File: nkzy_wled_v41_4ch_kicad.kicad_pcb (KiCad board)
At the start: 2 copper layers, 61 x 39 mm, 68 parts, among them CN1 1x3P_3.96mm_RA_Conn, CN2 1x3P_3.96mm_RA_Conn, CN3 1x3P_3.96mm_RA_Conn, CN4 1x3P_3.96mm_RA_Conn, CN5 1x2P_3.96mm_RA_Conn, J1 1x2P_2.54mm_RA_Conn, J2 HC-2510-3AW, K1 12VDC_SPDT, Q1 AO3401, U1 ESP32-WROOM-32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

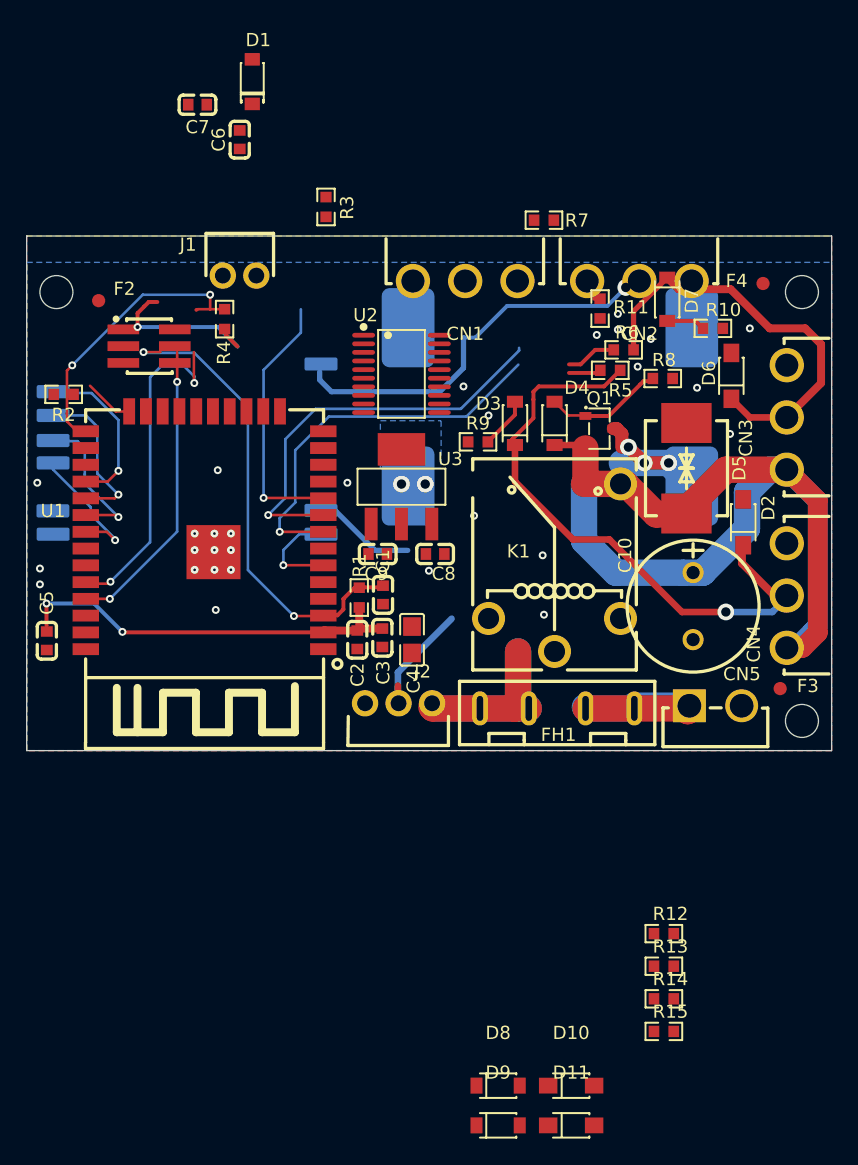
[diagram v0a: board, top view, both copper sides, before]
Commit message: Routed 4 ch pcb and resolved all DRC
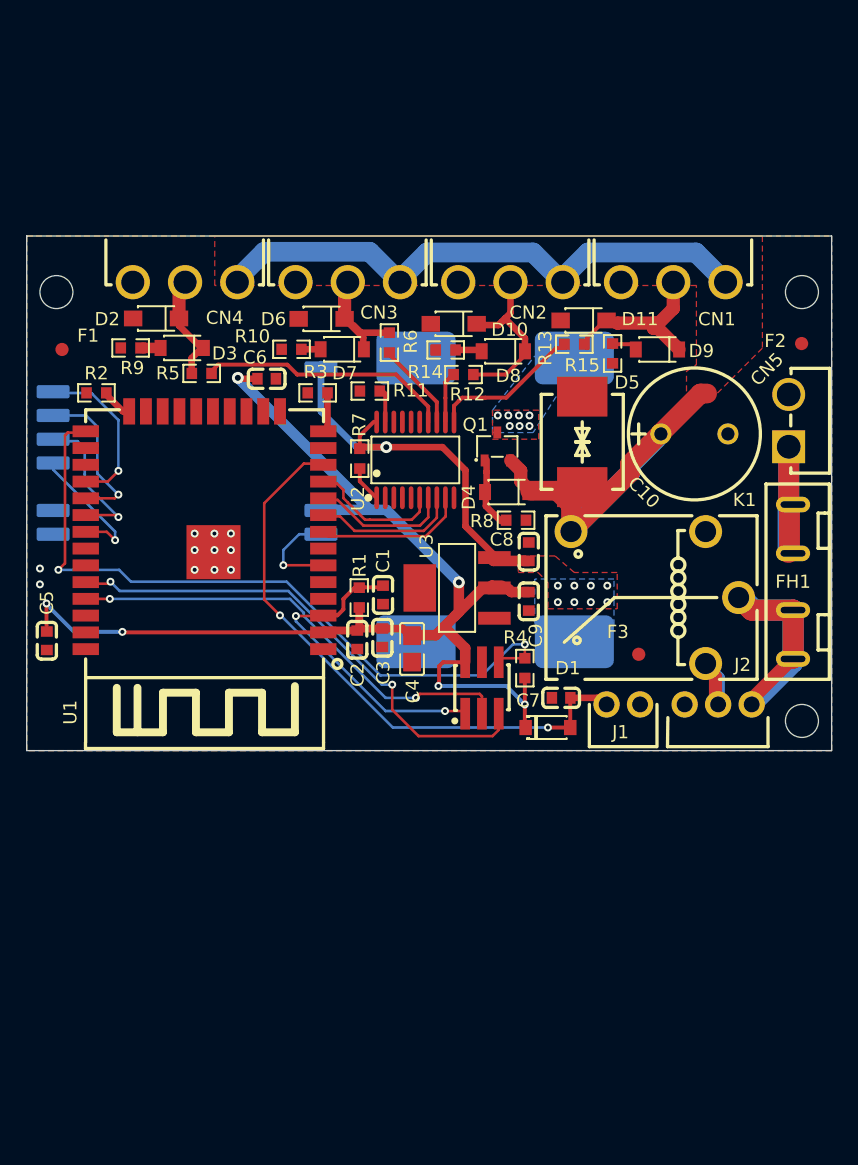
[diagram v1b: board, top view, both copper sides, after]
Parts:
- removed the F2 at (5.45, 2.90)
- removed P1, P2, P3, P4, P5, P6, P7, P8, P9: ~, nkzy_wled_lib:Pad_2.5x1mm
- added F1: Fiducial_1mm_Mask2mm, Fiducial:Fiducial_1mm_Mask2mm, F.Cu at (2.67, 6.60)
- added J3: ~, nkzy_wled_lib:nkzy_addon_footprint, B.Cu at (12.2, 14.3)
- moved D11 61.0 mm to (42.2, 4.40), turned to 180 degrees
- moved D9 60.0 mm to (47.8, 6.60), turned to 180 degrees
- moved D10 58.4 mm to (32.4, 4.65), turned to 180 degrees
- moved D8 55.7 mm to (36.1, 6.74), turned to 180 degrees
- moved D1 53.8 mm to (39.5, 35.2), turned to 0 degrees
- moved C7 52.7 mm to (40.5, 33.0)
- moved R14 51.9 mm to (31.8, 6.64)
- moved R15 51.5 mm to (44.4, 6.90), turned to 90 degrees
- moved CN4 51.4 mm to (12.0, 1.50), turned to 180 degrees
- moved R13 47.6 mm to (41.5, 6.20), turned to 180 degrees
- moved D2 47.1 mm to (9.80, 4.25), turned to 180 degrees
- moved R12 45.0 mm to (33.1, 8.50), turned to 180 degrees
- moved J1 43.6 mm to (45.2, 33.5), turned to 0 degrees
- moved H1 36.2 mm to (34.5, 32.2), turned to 0 degrees
- moved R4 34.9 mm to (37.8, 30.8)
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- renumbered F4 to F2
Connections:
- U1 pad 10: /Button_pin -> /CH3_MCU
- U1 pad 11: unconnected-(U1-IO26-Pad11) -> /CH4_MCU
- U1 pad 12: unconnected-(U1-IO27-Pad12) -> /Button_pin
- U1 pad 28: Net-(U1-IO17) -> /EXT_IO1
- U1 pad 29: Net-(U1-IO5) -> /EXT_IO2
- U1 pad 30: Net-(U1-IO18) -> /EXT_IO3
- U1 pad 31: Net-(U1-IO19) -> /EXT_IO4
- U1 pad 6: Net-(U1-IO34) -> /EXT_AIO_1
- U1 pad 8: /CH2_MCU -> /CH1_MCU
- U1 pad 9: /CH1_MCU -> /CH2_MCU
- U2 pad 11: /CH2_LevelShifted -> /CH1_LevelShifted
- U2 pad 12: /CH1_LevelShifted -> /CH2_LevelShifted
- U2 pad 8: /CH1_MCU -> /CH2_MCU
- U2 pad 9: /CH2_MCU -> /CH1_MCU
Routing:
- net +3.3V: track 39.0 -> 92.7 mm, vias 2 -> 6
- net Net-(D2-K): track 45.6 -> 7.85 mm, vias 1 -> 0
- net /ESP_IO0: track 21.4 -> 54.0 mm
- net /Button_pin: track 19.8 -> 45.0 mm, vias 1 -> 2
- net /ESP_EN: track 45.8 -> 22.5 mm, vias 3 -> 2
- net Net-(D6-K): track 31.7 -> 8.98 mm
- net /CH1_MCU: track 31.2 -> 11.0 mm, vias 1 -> 0
- net /CH2_MCU: track 29.6 -> 11.0 mm, vias 1 -> 0
- net /CH4_LevelShifted: track 2.46 -> 19.3 mm
- net /ESP_RX0: track 25.4 -> 38.6 mm
- net Net-(D10-K): track 0.00 -> 12.9 mm
- net Net-(D11-K): track 0.00 -> 12.4 mm
- net /ESP_TX0: track 22.3 -> 34.4 mm
- net Net-(U1-IO17): track 12.2 -> 0.00 mm, vias 1 -> 0
- net /EXT_IO1: track 0.00 -> 12.2 mm, vias 0 -> 1
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- added copper zone on F.Cu, net +5V
- added copper zone on B.Cu, net /VCC_IN_SAFE
- added copper zone on F.Cu, net /VCC_IN_SAFE
- added copper zone on F.Cu, net VCC_IN_SWITCHED
